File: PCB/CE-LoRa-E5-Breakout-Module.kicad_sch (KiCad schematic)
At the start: 26 parts, among them J1 Conn_01x12_Male, J2 Conn_01x12_Male, SW1 BOOT, SW2 RESET, U1 LoRa-E5, U2 3V3 LDO - SOT23

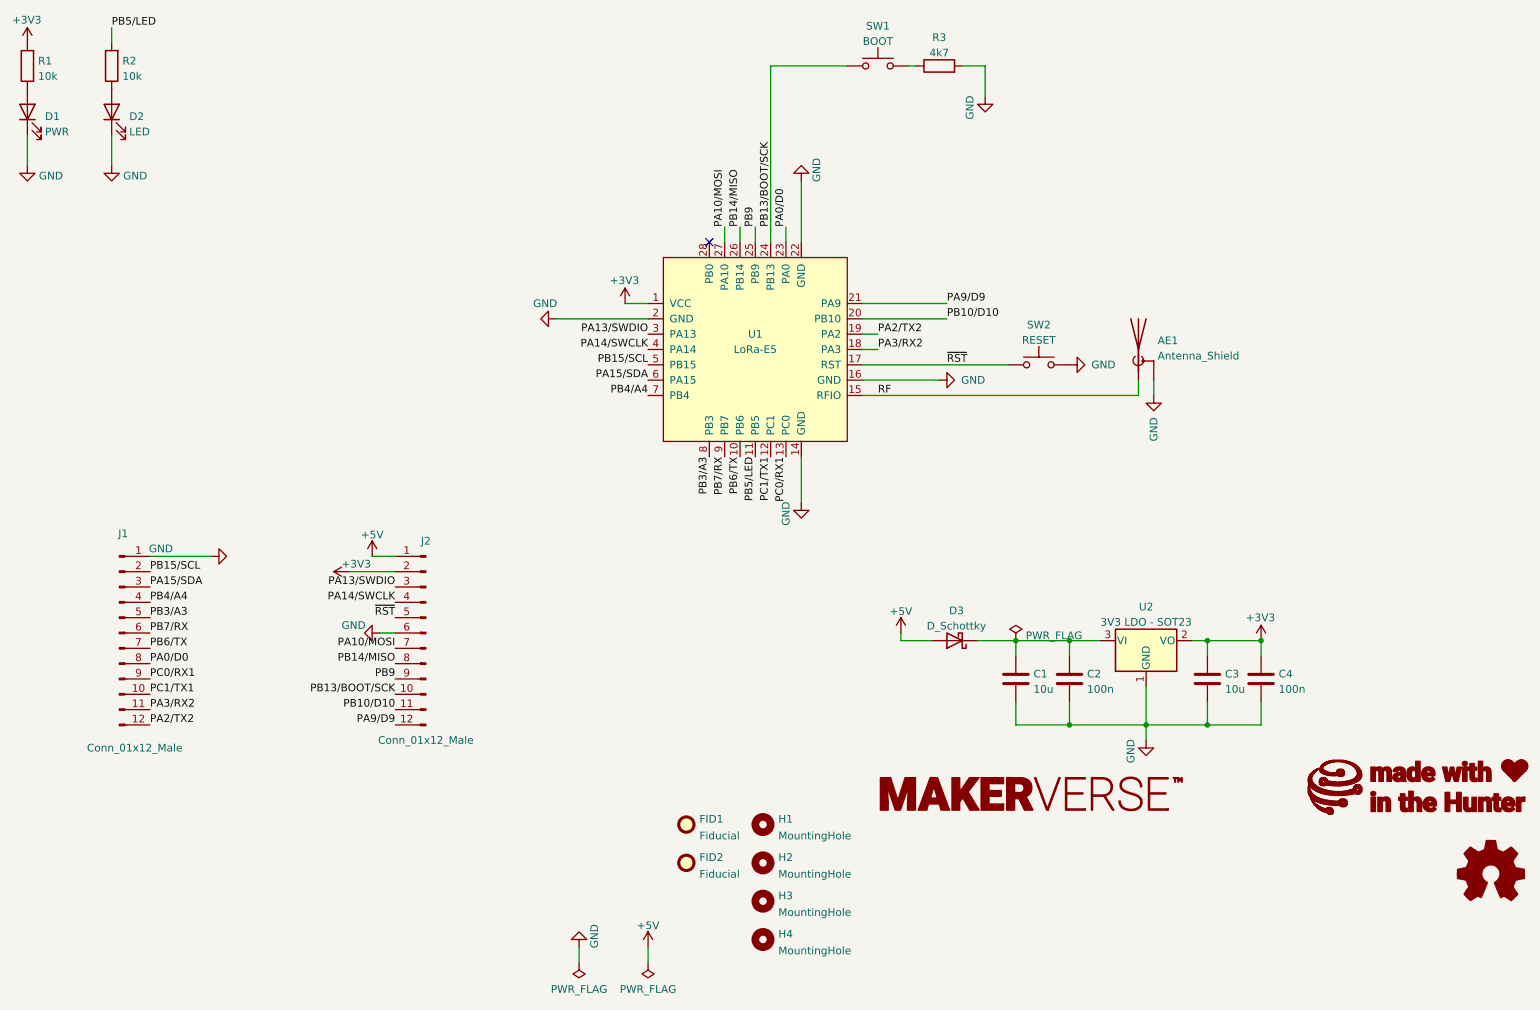
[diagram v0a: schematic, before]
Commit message: v02 prototype with SMA connector option
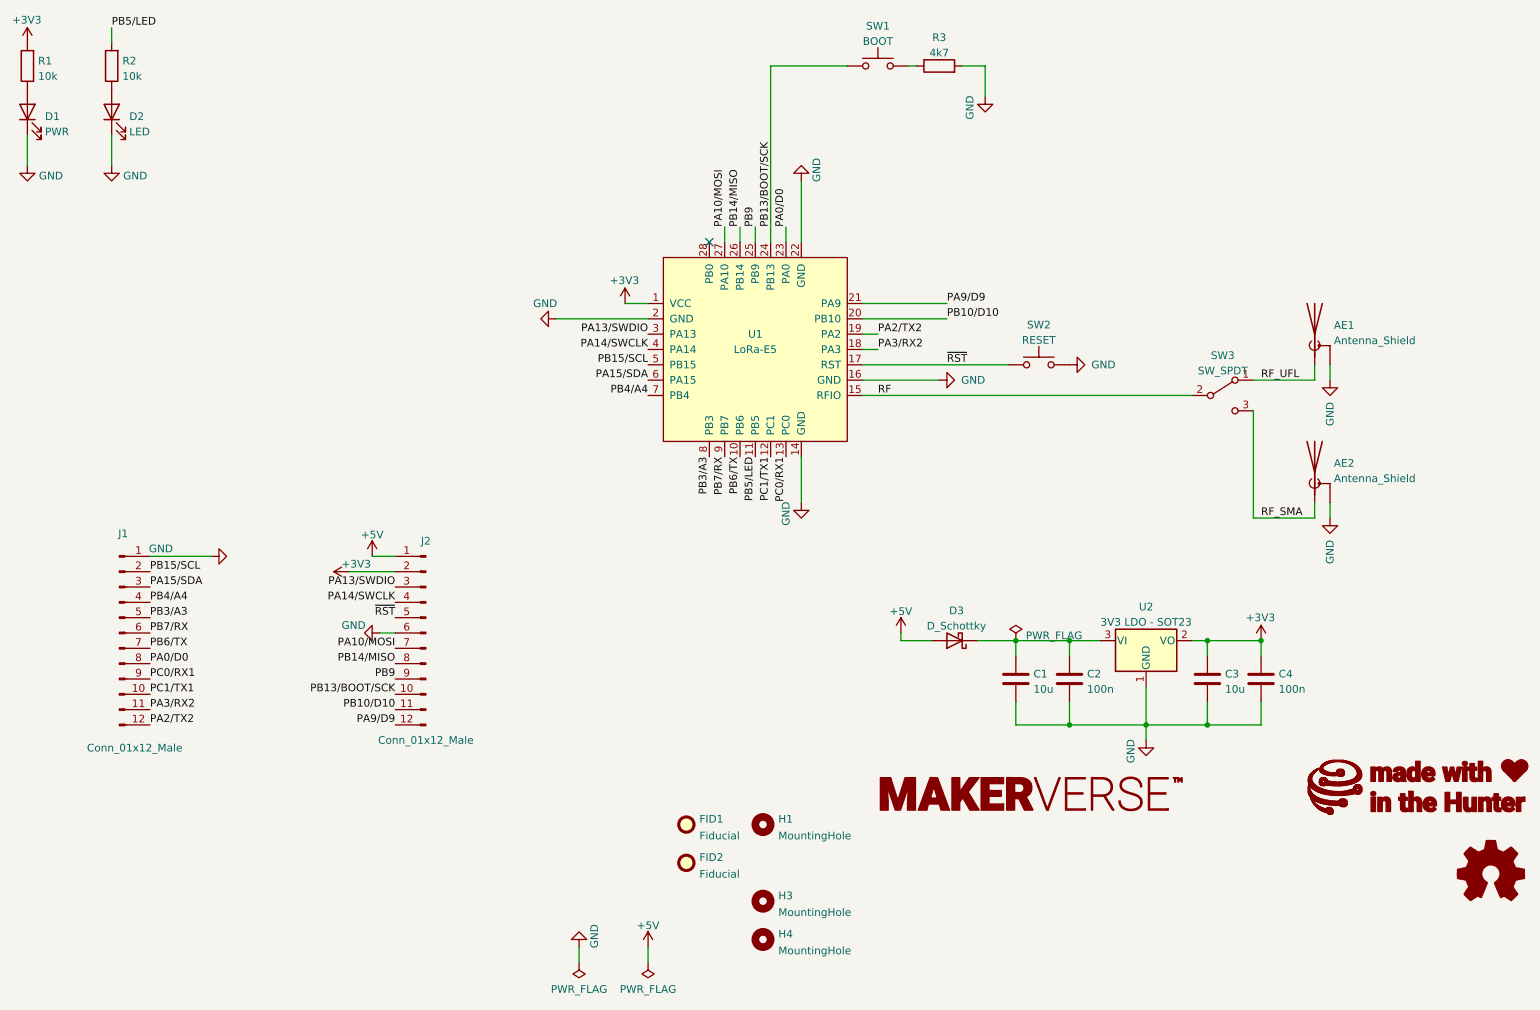
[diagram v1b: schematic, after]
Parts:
- removed H2: MountingHole, MountingHole:MountingHole_3.2mm_M3, symbol Mechanical:MountingHole
- added AE2: Antenna_Shield, CoreElectronics_Components:Conn_RF_SMA_EdgeMount, symbol Device:Antenna_Shield
- added SW3: SW_SPDT, CoreElectronics_Components:Jumper_Resistor_SPDT_0603_1608Metric, symbol Switch:SW_SPDT
- SW1, SW2: footprint Button_Switch_SMD:SW_SPST_TL3305A -> Button_Switch_SMD:SW_SPST_TL3342
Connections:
- net GND: now also AE2.2 (Shield)
- net RF: now also SW3.2 (B); no longer AE1.1 (A)
- new net RF_SMA: AE2.1 (A), SW3.3 (C)
- new net RF_UFL: AE1.1 (A), SW3.1 (A)
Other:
- moved on the sheet: AE1

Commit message: v10
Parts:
- AE1: value Antenna_Shield -> UFL
- AE2: value Antenna_Shield -> SMA
- R4: renamed from SW3; value SW_SPDT -> 0R; symbol Switch:SW_SPDT -> option-resistor:R_Option
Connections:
- net +3V3: now also D2.2 (A)
- net GND: no longer D2.1 (K)
- net at R2.1: now also D2.1 (K); no longer D2.2 (A)
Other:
- company: (none) -> Core Electronics
- title: (none) -> Makerverse LoRa-E5 Breakout
- moved on the sheet: D2, R2
